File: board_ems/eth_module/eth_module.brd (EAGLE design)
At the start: 68.6 x 54.3 mm, 46 parts, among them Q1 25MHz, U1 W5500, U2 ARDUINOR3-DIMENSION

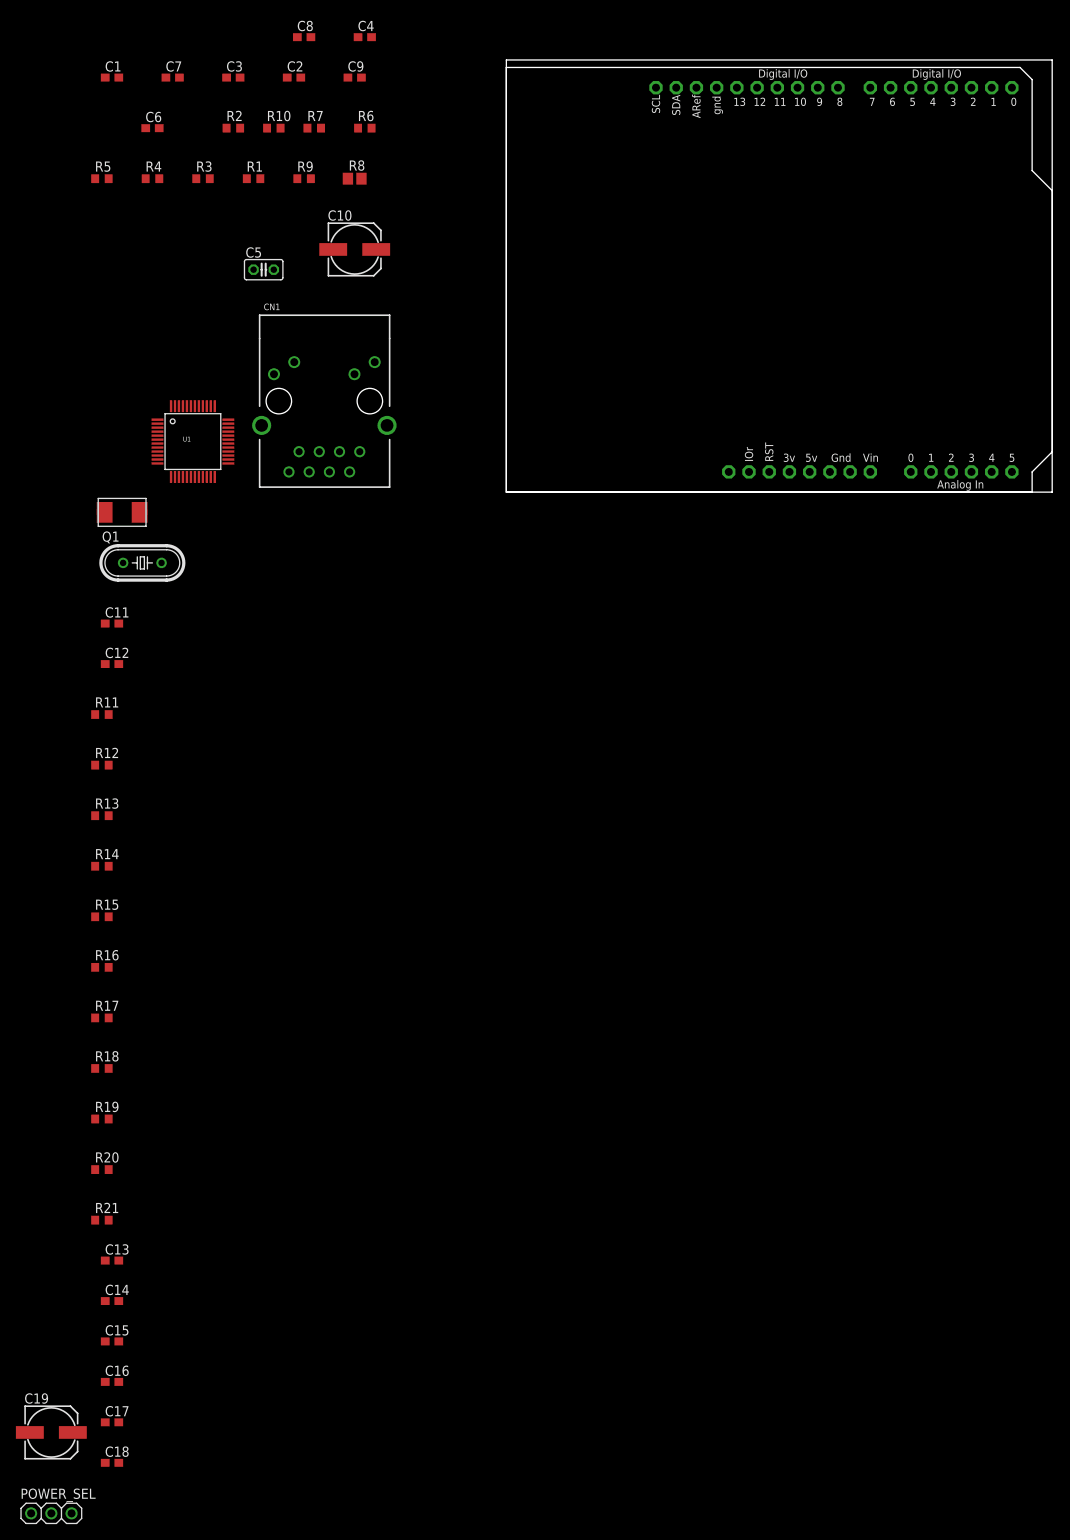
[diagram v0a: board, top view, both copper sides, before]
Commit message: add eth_module
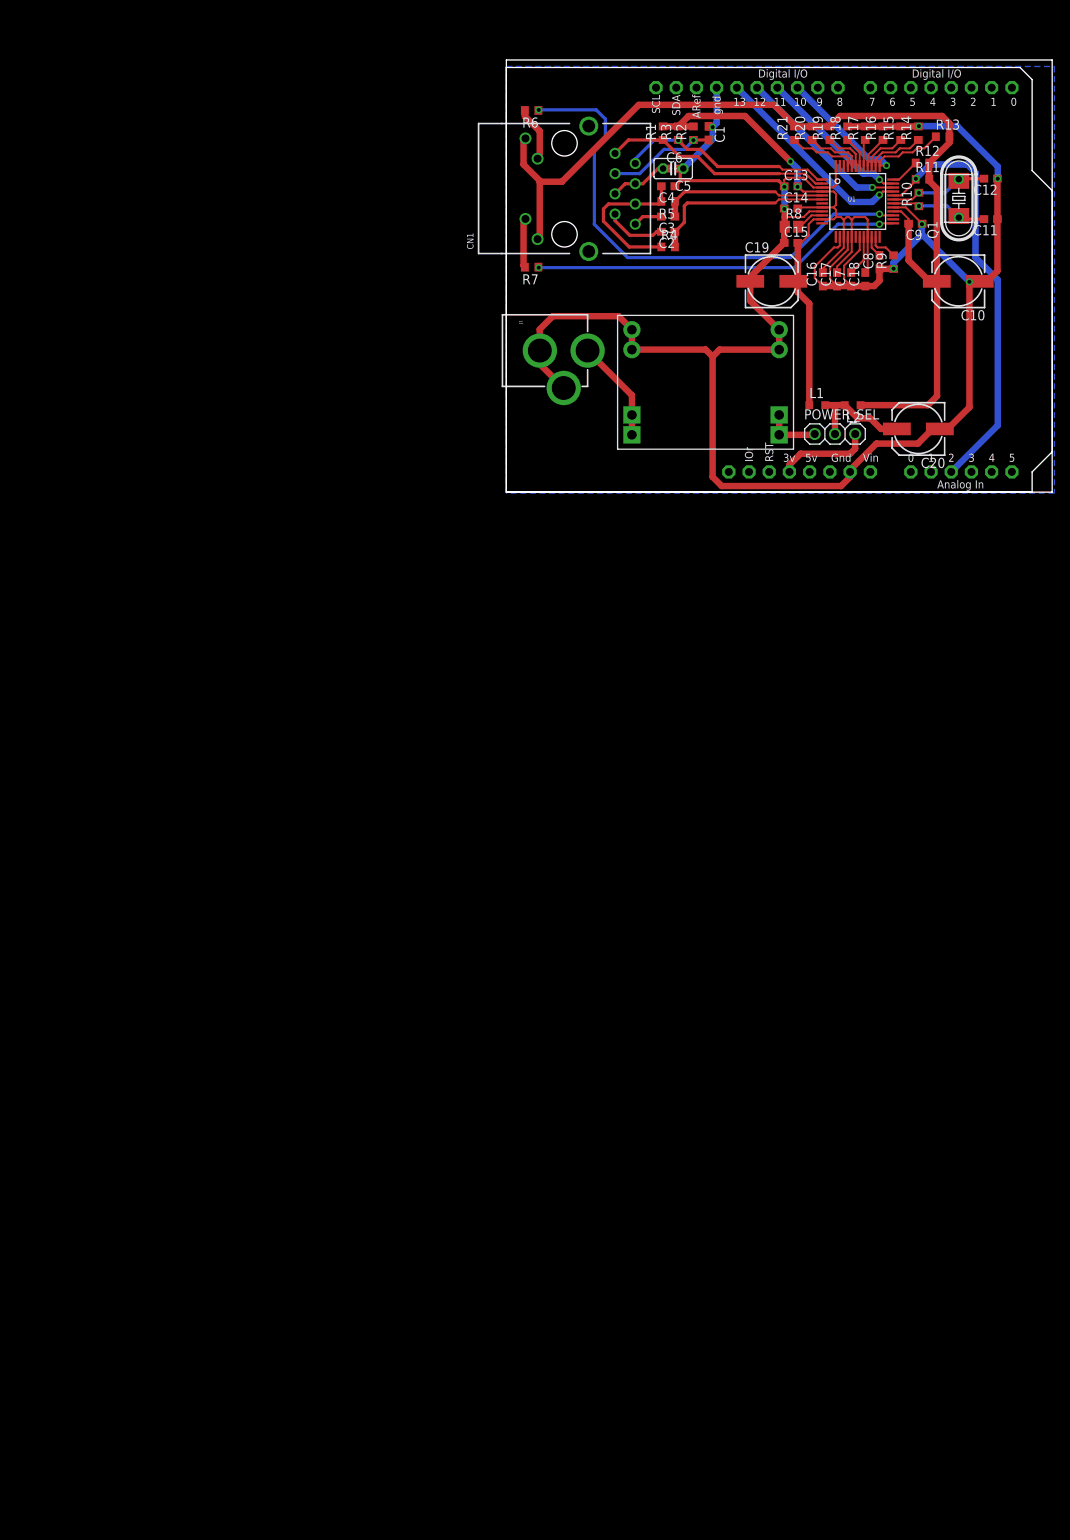
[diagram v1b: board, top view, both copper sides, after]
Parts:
- added C20: C10uF/16V, resistor:153CLV-0605
- added J1: POWER_JACKPTH, SparkFun-Connectors:POWER_JACK_PTH
- added L1, L2: (no value), resistor:L2012C
- added U$2: DCDCMODULE_SMALL, bontor:DCDCMODULE-SMALL
- moved C18 176.2 mm to (45.1, 26.7), turned to 90 degrees
- moved C19 170.6 mm to (33.3, 26.5)
- moved C17 170.0 mm to (41.5, 26.7), turned to 90 degrees
- moved POWER_SEL 167.5 mm to (41.3, 7.30)
- moved C16 164.8 mm to (39.8, 26.7), turned to 90 degrees
- moved C15 162.2 mm to (35.8, 31.3)
- moved R21 161.9 mm to (36.2, 45.1), turned to 90 degrees
- moved C14 161.6 mm to (35.8, 35.6)
- moved C13 159.6 mm to (35.8, 38.4)
- moved R20 157.8 mm to (38.4, 45.1), turned to 90 degrees
- moved R19 153.9 mm to (40.6, 45.1), turned to 90 degrees
- moved R18 150.2 mm to (42.9, 45.1), turned to 90 degrees
- moved R17 146.8 mm to (45.1, 45.1), turned to 90 degrees
- moved R16 143.5 mm to (47.3, 45.1), turned to 90 degrees
- moved R15 140.5 mm to (49.5, 45.1), turned to 90 degrees
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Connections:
- net 5V renamed 5VPS
- removed net 3V3_ARDU: U2.3V
- new net PWRIN: J1.PWR, U$2.INP#1, U$2.INP#2
- net 3V3A: now also L1.1
- net 3V3ARDU: now also U2.3V
- net 3V3D: now also L2.1
- net 3V3IN: now also C20.+, L1.2, L2.2
- net 3V3PS: now also U$2.OUTP#1, U$2.OUTP#2
- net GND: now also C20.-, J1.GND, J1.GNDBREAK, U$2.INM#1, U$2.INM#2, U$2.OUTM#1, U$2.OUTM#2
- net MISO: now also U2.D12
- net MOSI: now also U2.D11
- net SCLK: now also U2.D13
- net SCSN: now also U2.A2
- net W5500_NRST: now also U2.D10
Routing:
- net GND: track 0.00 -> 271.7 mm, vias 0 -> 8
- net 3V3D: track 0.00 -> 129.4 mm
- net 3V3A: track 0.00 -> 92.6 mm, vias 0 -> 2
- net ACTLED: track 0.00 -> 64.3 mm, vias 0 -> 2
- net SCSN: track 0.00 -> 53.7 mm, vias 0 -> 1
- net LINKLED: track 0.00 -> 46.9 mm, vias 0 -> 2
- net TXP: track 0.00 -> 29.0 mm
- net TXN: track 0.00 -> 27.2 mm, vias 0 -> 1
- net SCLK: track 0.00 -> 26.1 mm, vias 0 -> 1
- net W5500_NRST: track 0.00 -> 25.1 mm, vias 0 -> 1
- net RXP: track 0.00 -> 23.3 mm
- net MISO: track 0.00 -> 22.3 mm, vias 0 -> 1
- net RXN: track 0.00 -> 21.1 mm
- net N$6: track 0.00 -> 19.7 mm
- net MOSI: track 0.00 -> 19.5 mm, vias 0 -> 1
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- added copper zone on layer 16, net GND
